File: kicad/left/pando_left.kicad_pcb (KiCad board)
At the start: 2 copper layers, 144.1 x 121.5 mm, 93 parts, among them J1 USB_C_Receptacle_USB2.0_14P, J2 USB_C_Receptacle_USB2.0_14P, U1 STM32F072CBT6, U2 PRTR5V0U2X, U3 XC6206PxxxMR-Regulator_Linear, U4 PRTR5V0U2X

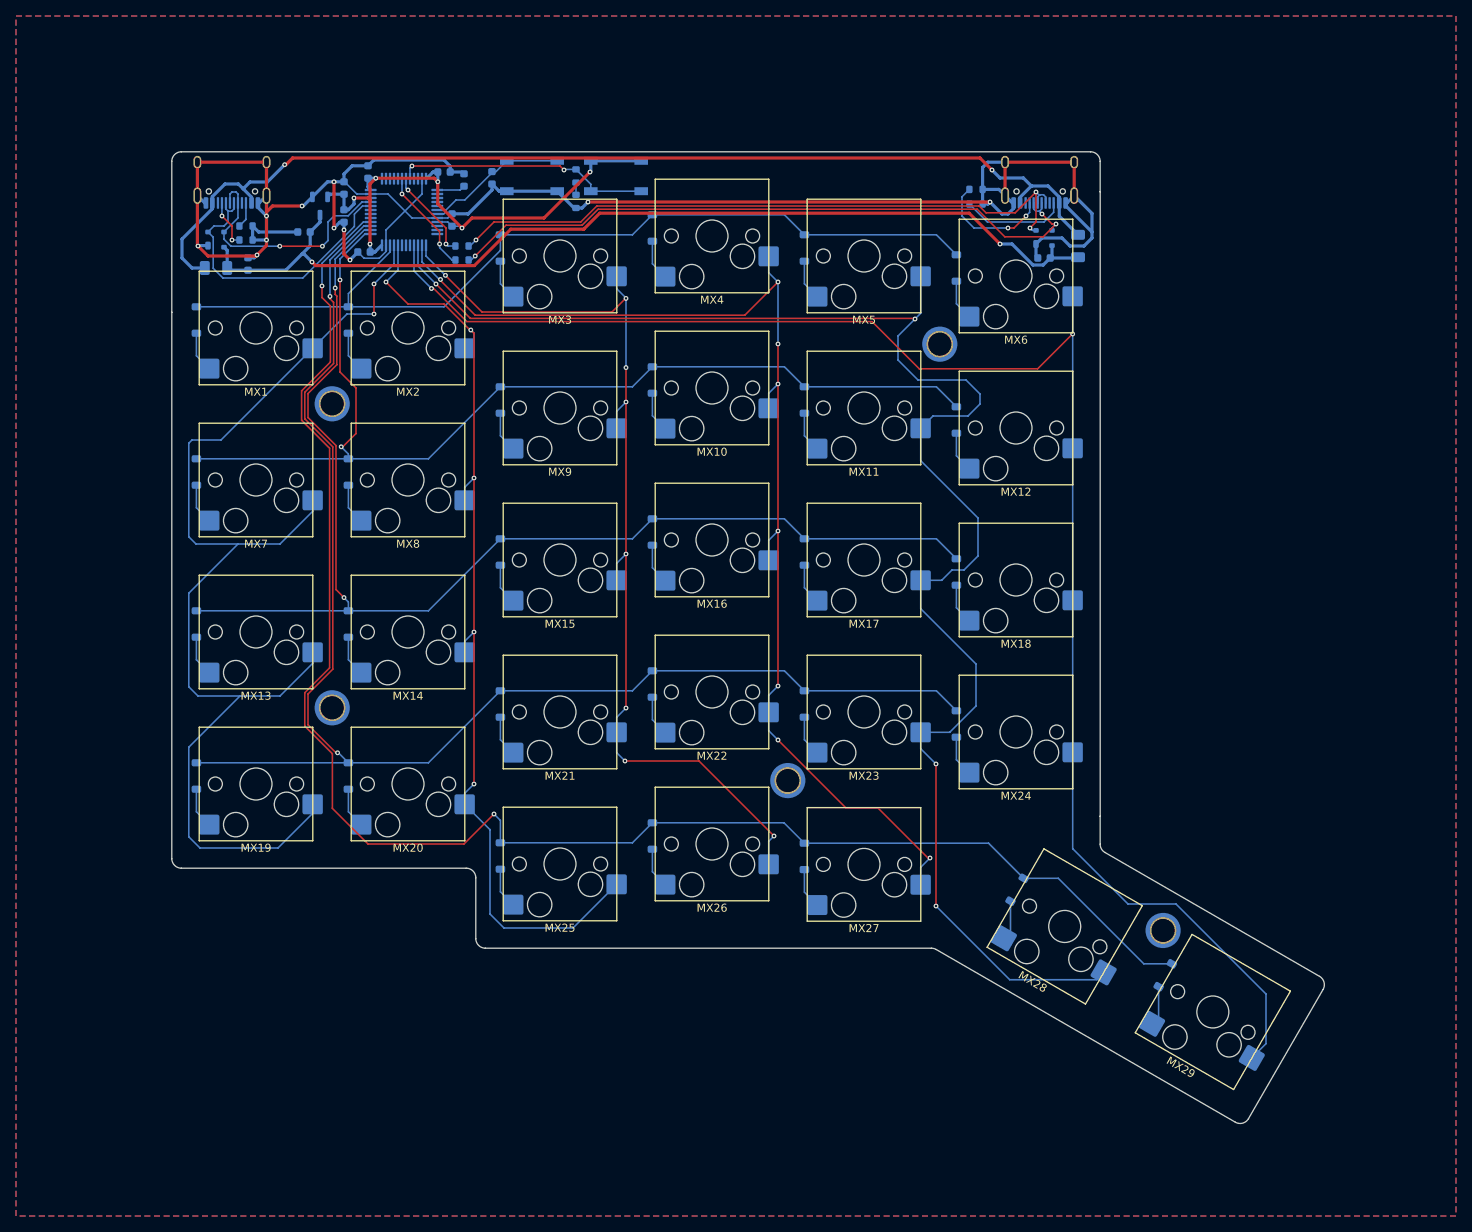
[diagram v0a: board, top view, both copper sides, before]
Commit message: v1.1.0: Fix I2C pull-up routing and clean up traces
- Reposition I2C pull-up resistors R7/R8 with VBUS connections
- Clean up DATA0/DATA1 label positions and wire routing
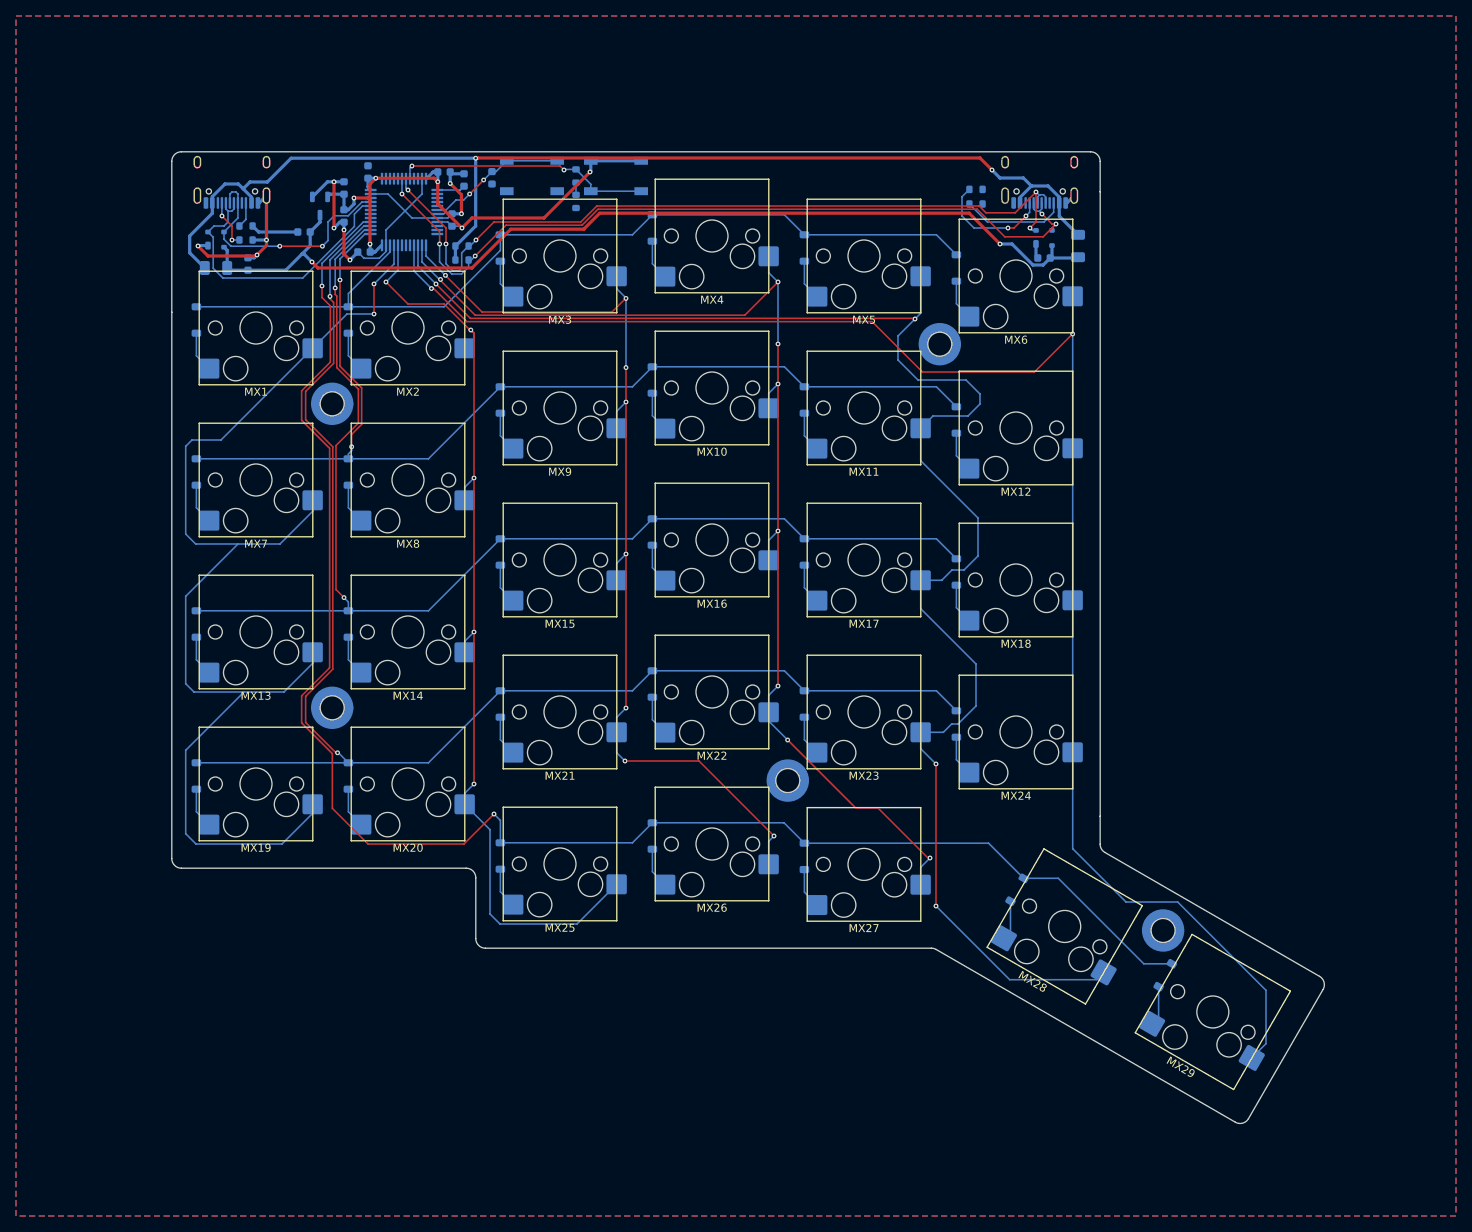
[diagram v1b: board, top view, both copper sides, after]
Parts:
- H1, H2, H3, H4, H5: footprint Pando:MountingHole_2.9mm_M2_Pad_TopOnly -> Mounting_Wuerth:Mounting_Wuerth_WA-SMSI-M2_H3.5mm_9774035243
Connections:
- R7 pad 1: Net-(U1-PB6) -> VBUS
- R8 pad 1: Net-(U1-PB7) -> VBUS
- U1 pad 42: Net-(U1-PB6) -> DATA0
- U1 pad 43: Net-(U1-PB7) -> DATA1
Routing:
- net GND: track 256.5 -> 84.2 mm, vias 11 -> 9
- net DATA1: track 83.3 -> 101.6 mm, vias 3 -> 5
- net DATA0: track 84.6 -> 102.5 mm, vias 3 -> 5
- net Net-(U1-PB6): track 13.2 -> 0.00 mm, vias 2 -> 0
- net VBUS: track 133.6 -> 145.6 mm
- net Net-(U1-PB7): track 11.5 -> 0.00 mm, vias 2 -> 0
- net COL3: track 149.6 -> 147.9 mm
- net COL0: track 147.6 -> 148.5 mm
- net ROW2: track 155.4 -> 154.7 mm
- net COL5: track 201.9 -> 202.5 mm
- net NRST: track 17.8 -> 17.9 mm, vias 0 -> 2
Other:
- board text added: "Designed in Washington, USA - by jyap - v1.1"
- board text removed: "Designed in Washington, USA - by jyap - v1.0"

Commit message: Update left PCB and schematic for STM32G0B1CBT6
Replace STM32F072CBT6 with STM32G0B1CBT6 MCU. Update routing
and schematics to match new pinout and requirements.
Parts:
- removed C5, C6, C7: 100nF, Capacitor_SMD:C_0603_1608Metric
- U1: value STM32F072CBT6 -> STM32G0B1CBT6
- moved C2 14.7 mm to (172.0, 95.8), turned to 0 degrees
- moved C4 13.3 mm to (172.0, 99.2), turned to 0 degrees
- moved C3 12.1 mm to (172.0, 97.5), turned to 0 degrees
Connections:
- U1 pad 1: +3V3 -> unconnected-(U1-PC13-Pad1)
- U1 pad 10: unconnected-(U1-PA0-Pad10) -> NRST
- U1 pad 17: unconnected-(U1-PA7-Pad17) -> COL1
- U1 pad 18: unconnected-(U1-PB0-Pad18) -> COL0
- U1 pad 20: COL1 -> unconnected-(U1-PB1-Pad20)
- U1 pad 21: COL0 -> unconnected-(U1-PB2-Pad21)
- U1 pad 22: ROW0 -> unconnected-(U1-PB10-Pad22)
- U1 pad 23: GND -> unconnected-(U1-PB11-Pad23)
- U1 pad 24: +3V3 -> ROW0
- U1 pad 32: D- -> unconnected-(U1-PA10/UCPD1_DBCC2-Pad32)
- U1 pad 33: D+ -> D-
- U1 pad 34: unconnected-(U1-PA13-Pad34) -> D+
- U1 pad 35: GND -> unconnected-(U1-PA13-Pad35)
- U1 pad 36: +3V3 -> BOOT0
- U1 pad 4: unconnected-(U1-PC15-Pad4) -> +3V3
- U1 pad 42: DATA0 -> unconnected-(U1-PB3-Pad42)
- U1 pad 43: DATA1 -> unconnected-(U1-PB4-Pad43)
- U1 pad 44: BOOT0 -> unconnected-(U1-PB5-Pad44)
- U1 pad 45: unconnected-(U1-PB8-Pad45) -> DATA1
- U1 pad 46: unconnected-(U1-PB9-Pad46) -> DATA0
- U1 pad 47: GND -> unconnected-(U1-PB8-Pad47)
- U1 pad 48: +3V3 -> unconnected-(U1-PB9-Pad48)
- U1 pad 5: unconnected-(U1-PF0-Pad5) -> +3V3
- U1 pad 6: unconnected-(U1-PF1-Pad6) -> +3V3
- U1 pad 7: NRST -> GND
- U1 pad 8: GND -> unconnected-(U1-PF0-Pad8)
- U1 pad 9: +3V3 -> unconnected-(U1-PF1-Pad9)
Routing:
- net GND: track 84.2 -> 55.4 mm, vias 9 -> 7
- net +3V3: track 75.0 -> 64.5 mm, vias 6 -> 3
- net BOOT0: track 32.2 -> 38.6 mm
- net NRST: track 17.9 -> 23.9 mm
- net COL1: track 119.6 -> 115.6 mm
- net VBUS: track 145.6 -> 146.9 mm
- net DATA0: track 102.5 -> 101.7 mm
- net COL0: track 148.5 -> 149.1 mm

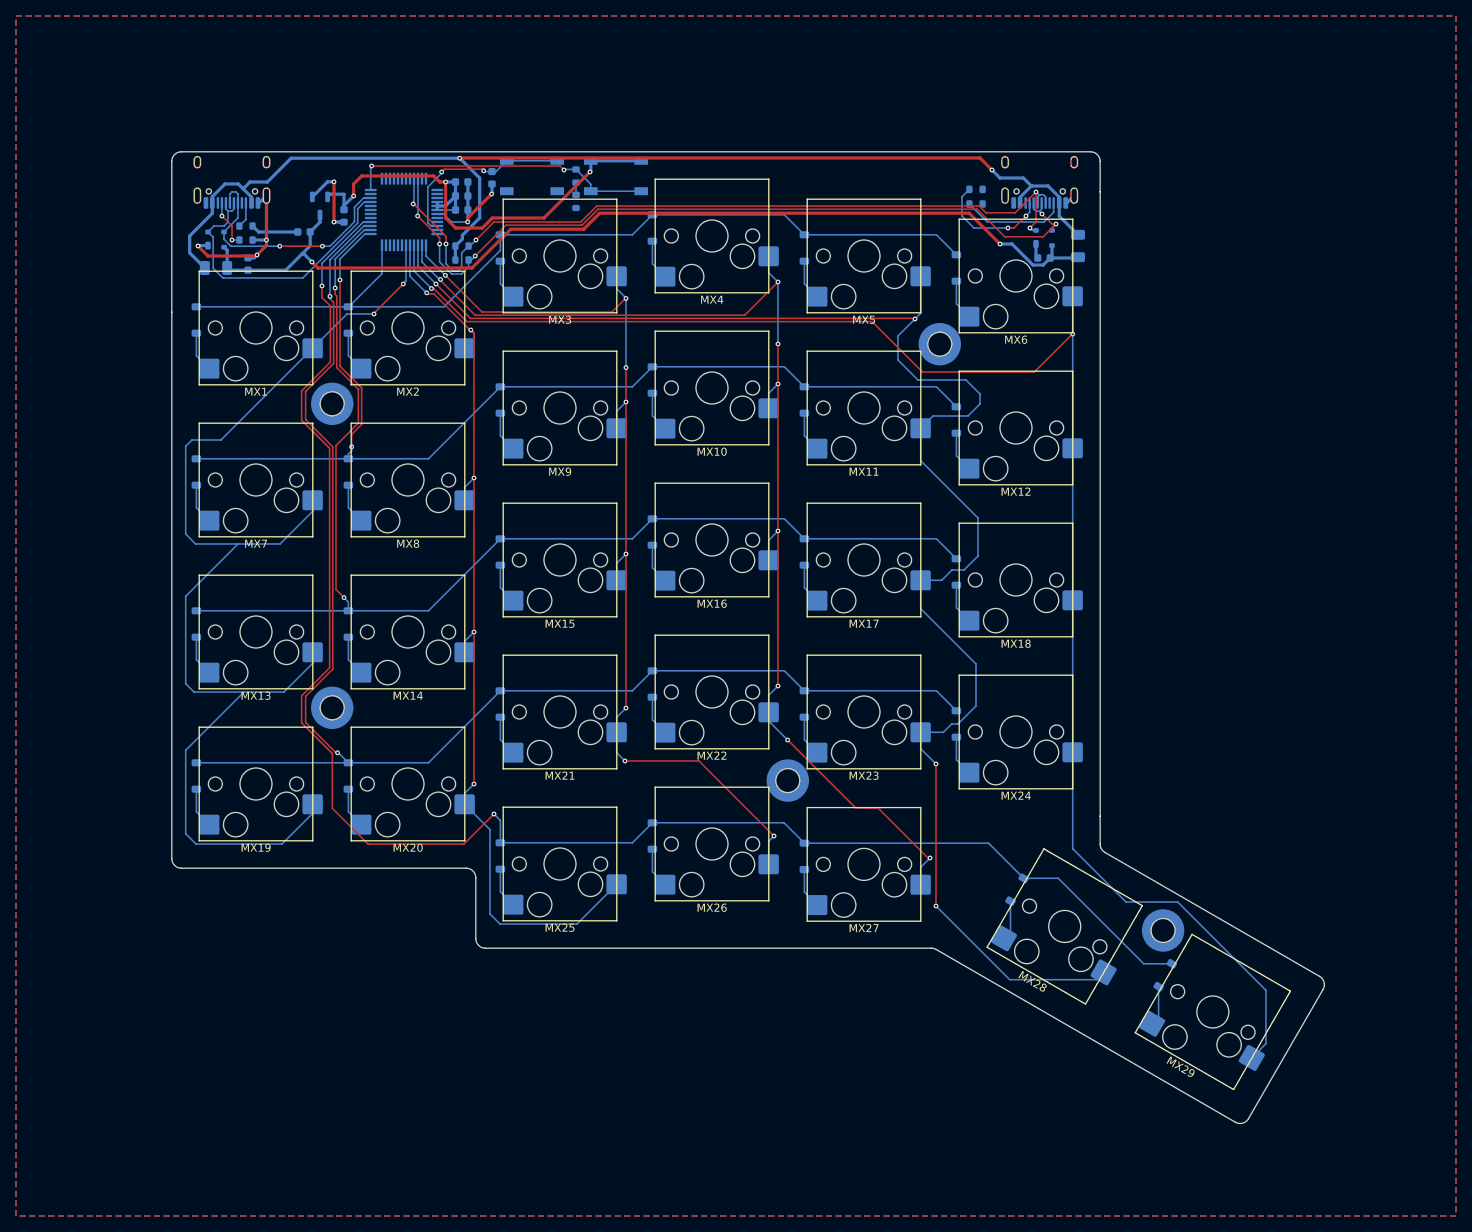
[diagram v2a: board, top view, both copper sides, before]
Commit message: Update left PCB and schematic for STM32G0B1KBT6
Replace STM32G0B1CBT6 with STM32G0B1KBT6 MCU. Update routing
and schematics to match new pinout and requirements.
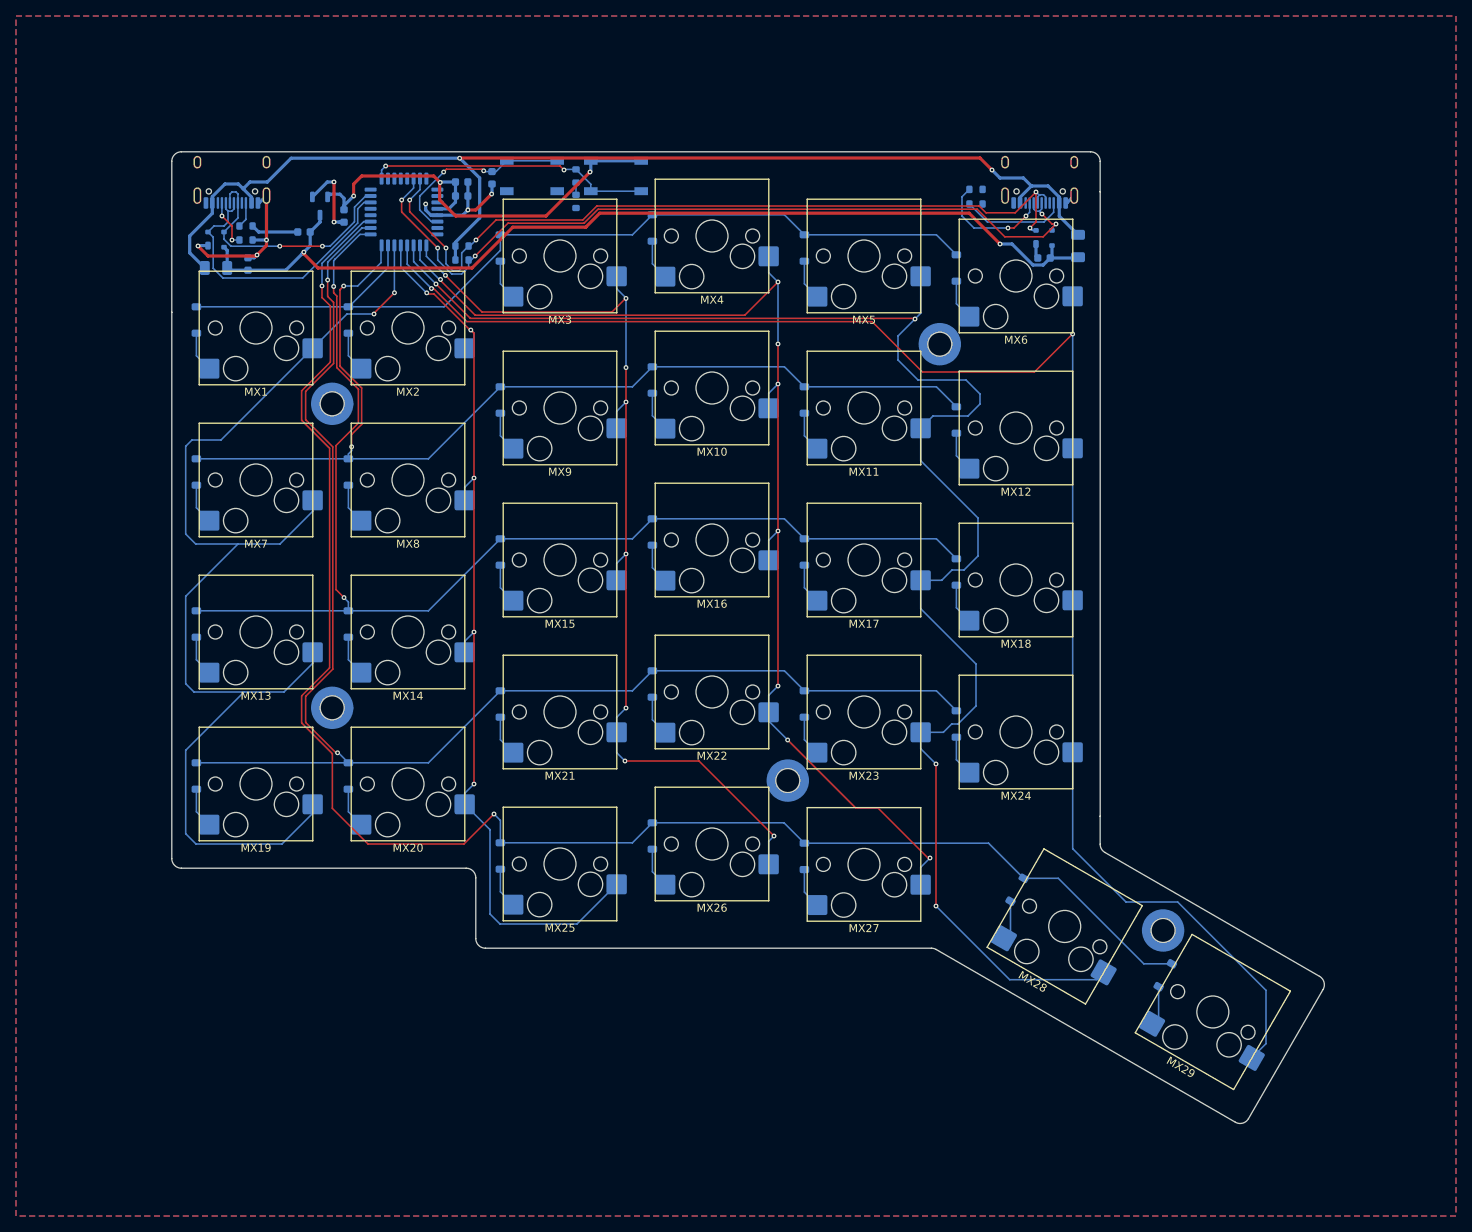
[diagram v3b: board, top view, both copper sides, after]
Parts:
- removed C4: 100nF, Capacitor_SMD:C_0603_1608Metric
- U1: value STM32G0B1CBT6 -> STM32G0B1KBT6; footprint Package_QFP:LQFP-48_7x7mm_P0.5mm -> Package_QFP:LQFP-32_7x7mm_P0.8mm
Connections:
- U1 pad 10: NRST -> COL3
- U1 pad 11: unconnected-(U1-PA0-Pad11) -> COL4
- U1 pad 12: unconnected-(U1-PA1-Pad12) -> COL5
- U1 pad 13: COL2 -> COL1
- U1 pad 14: COL3 -> COL0
- U1 pad 15: COL4 -> ROW0
- U1 pad 16: COL5 -> ROW1
- U1 pad 17: COL1 -> ROW2
- U1 pad 18: COL0 -> ROW3
- U1 pad 19: unconnected-(U1-PB0-Pad19) -> ROW4
- U1 pad 22: unconnected-(U1-PB10-Pad22) -> D-
- U1 pad 23: unconnected-(U1-PB11-Pad23) -> D+
- U1 pad 24: ROW0 -> unconnected-(U1-PA13-Pad24)
- U1 pad 25: ROW1 -> BOOT0
- U1 pad 26: ROW2 -> unconnected-(U1-PA15-Pad26)
- U1 pad 27: ROW3 -> unconnected-(U1-PB3-Pad27)
- U1 pad 28: ROW4 -> unconnected-(U1-PB4-Pad28)
- U1 pad 30: unconnected-(U1-PC6-Pad30) -> DATA0
- U1 pad 31: unconnected-(U1-PC7-Pad31) -> DATA1
- U1 pad 5: +3V3 -> GND
- U1 pad 6: +3V3 -> NRST
- U1 pad 7: GND -> unconnected-(U1-PA0-Pad7)
- U1 pad 9: unconnected-(U1-PF1-Pad9) -> COL2
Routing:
- net +3V3: track 64.5 -> 58.0 mm
- net BOOT0: track 38.6 -> 35.6 mm
- net DATA0: track 101.7 -> 103.1 mm
- net DATA1: track 101.3 -> 101.9 mm
- net COL0: track 149.1 -> 148.5 mm
- net D+: track 31.0 -> 30.4 mm
- net GND: track 55.4 -> 55.3 mm, vias 7 -> 8
